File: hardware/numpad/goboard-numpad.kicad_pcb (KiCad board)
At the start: 2 copper layers, 76.3 x 110.3 mm, 45 parts, among them J1 Conn_02x05_Top_Bottom, J2 Conn_01x01, J3 Conn_01x05, SW1 SW_Push, SW10 5, SW12 2, SW13 dot, SW14 times, SW15 9, SW16 6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

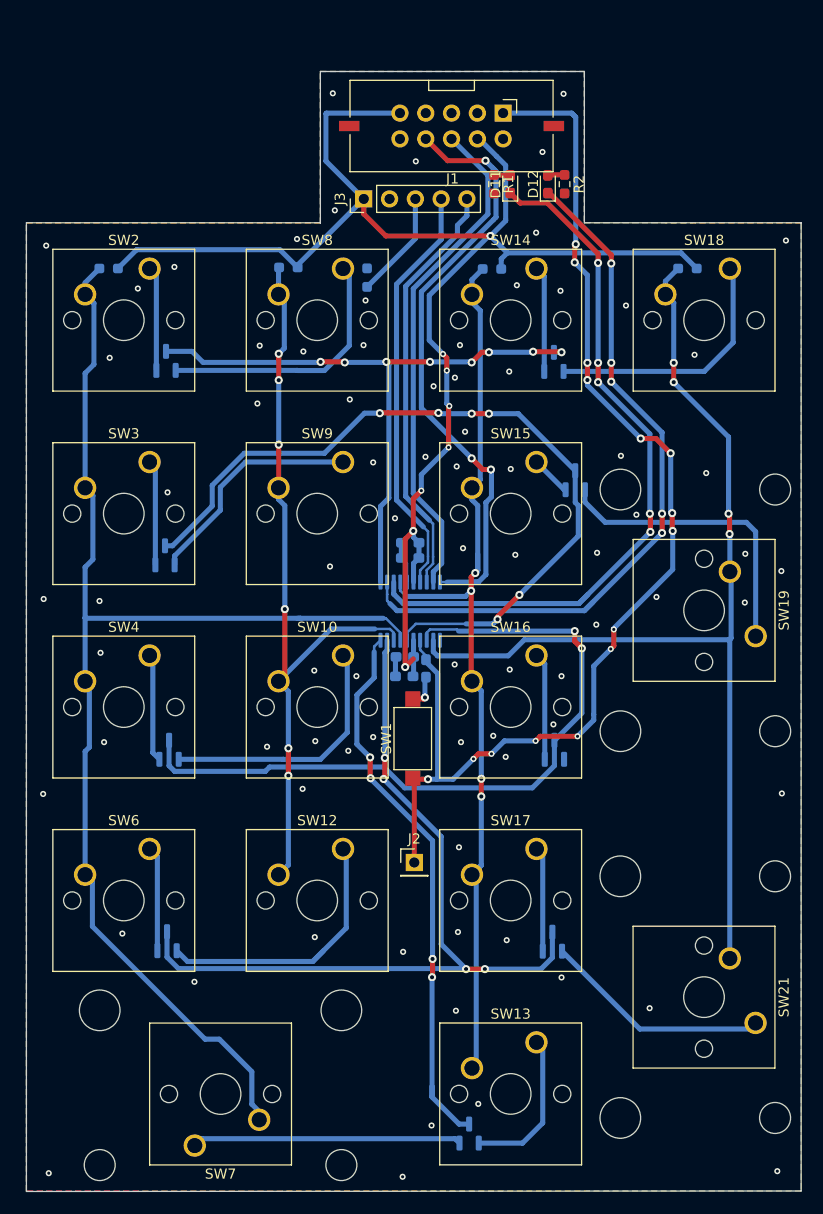
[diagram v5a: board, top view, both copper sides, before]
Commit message: Numpad: Fix DRC errors
Mainly placement of silkscreen content, track clearance violations and
overlapping courtyards.
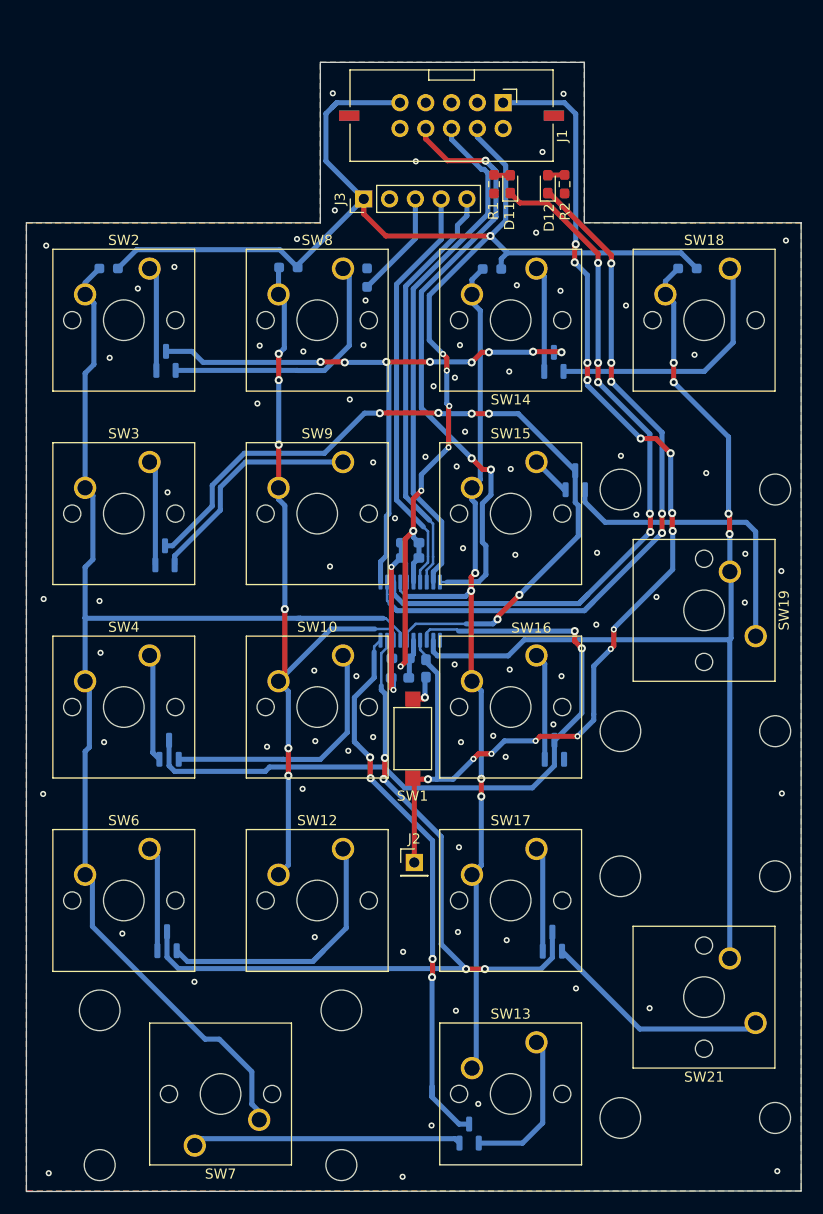
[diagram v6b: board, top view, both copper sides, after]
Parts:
- moved J1 1.02 mm to (151.5, 45.6)
- moved C5 0.45 mm to (141.3, 102.2)
- moved C2 0.45 mm to (141.4, 100.3)
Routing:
- net GND: track 9.35 -> 24.2 mm, vias 81 -> 83
- net /Keys/COLUMN_2: track 91.8 -> 90.0 mm
- net /SWDCLK: track 60.0 -> 61.3 mm
- net VCC: track 154.8 -> 156.0 mm
- net /SWDIO: track 49.7 -> 50.9 mm
- net /Keys/ROW_4: track 54.9 -> 55.4 mm
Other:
- board size 76.3 x 110.3 mm -> 76.3 x 111.2 mm

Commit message: Numpad: Fix position of the power-led
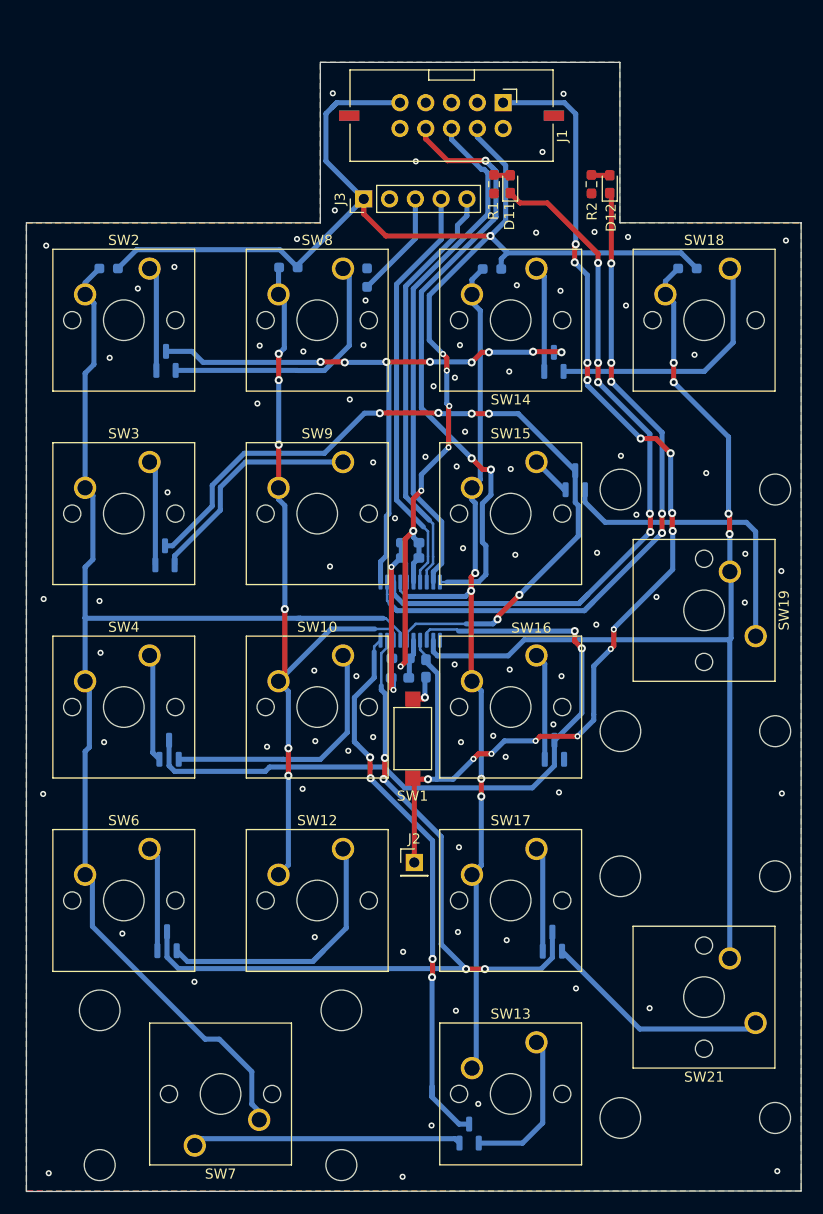
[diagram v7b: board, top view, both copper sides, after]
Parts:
- moved D12 6.10 mm to (162.0, 53.6)
- moved R2 2.65 mm to (160.2, 53.6)
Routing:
- net /mcu/LED_POWER: track 71.9 -> 69.3 mm
- net GND: vias 83 -> 86
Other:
- outline, holes or cut-outs redrawn
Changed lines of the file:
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@@
   )
   (footprint "Resistor_SMD:R_0603_1608Metric_Pad0.98x0.95mm_HandSolder" (layer "F.Cu")
-    (at 157.55 53.6 -90)
+    (at 160.2 53.6 -90)
     (descr "Resistor SMD 0603 (1608 Metric), square (rectangular) end terminal, IPC_7351 nominal with elongated pad for handsoldering. (Body size source: IPC-SM-782 page 72, https://www.pcb-3d.com/wordpress/wp-content/uploads/ipc-sm-782a_amendment_1_and_2.pdf), generated with kicad-footprint-generator")
     (tags "resistor handsolder")
@@
   )
   (footprint "Diode_SMD:D_0603_1608Metric_Pad1.05x0.95mm_HandSolder" (layer "F.Cu")
-    (at 155.9 53.6 90)
+    (at 162 53.6 90)
     (descr "Diode SMD 0603 (1608 Metric), square (rectangular) end terminal, IPC_7351 nominal, (Body size source: http://www.tortai-tech.com/upload/download/2011102023233369053.pdf), generated with kicad-footprint-generator")
     (tags "diode handsolder")
@@
   (gr_line (start 133.5 57.4) (end 104.55 57.4) (layer "Edge.Cuts") (width 0.1))
   (gr_line (start 133.5 41.6) (end 133.5 57.4) (layer "Edge.Cuts") (width 0.1))
-  (gr_line (start 159.5 57.4) (end 159.5 41.6) (layer "Edge.Cuts") (width 0.1))
-  (gr_line (start 159.5 41.6) (end 133.5 41.6) (layer "Edge.Cuts") (width 0.1))
+  (gr_line (start 163 57.4) (end 163 41.6) (layer "Edge.Cuts") (width 0.1))
+  (gr_line (start 163 41.6) (end 133.5 41.6) (layer "Edge.Cuts") (width 0.1))
   (gr_line (start 104.55 57.4) (end 104.55 152.8) (layer "Edge.Cuts") (width 0.1))
   (gr_line (start 180.85 152.75) (end 180.85 57.4) (layer "Edge.Cuts") (width 0.1))
-  (gr_line (start 180.85 57.4) (end 159.5 57.4) (layer "Edge.Cuts") (width 0.1))
+  (gr_line (start 180.85 57.4) (end 163 57.4) (layer "Edge.Cuts") (width 0.1))
   (segment (start 131.55 96.35) (end 131.25 96.35) (width 0.5) (layer "B.Cu") (net 1))
   (segment (start 110.33125 72.21875) (end 111.2 71.35) (width 0.5) (layer "B.Cu") (net 1))
@@
   (via (at 121.1 132.15) (size 0.6) (drill 0.3) (layers "F.Cu" "B.Cu") (free) (net 28))
   (via (at 147.55 89.45) (size 0.6) (drill 0.3) (layers "F.Cu" "B.Cu") (free) (net 28))
+  (via (at 157 113.5) (size 0.6) (drill 0.3) (layers "F.Cu" "B.Cu") (free) (net 28))
   (via (at 141.6 151.35) (size 0.6) (drill 0.3) (layers "F.Cu" "B.Cu") (free) (net 28))
   (via (at 147.75 77.975) (size 0.6) (drill 0.3) (layers "F.Cu" "B.Cu") (free) (net 28))
@@
   (via (at 179.35 59.15) (size 0.6) (drill 0.3) (layers "F.Cu" "B.Cu") (free) (net 28))
   (via (at 131.75 113.15) (size 0.6) (drill 0.3) (layers "F.Cu" "B.Cu") (free) (net 28))
+  (via (at 160.5 58.3) (size 0.6) (drill 0.3) (layers "F.Cu" "B.Cu") (free) (net 28))
   (via (at 171.5 82.05) (size 0.6) (drill 0.3) (layers "F.Cu" "B.Cu") (free) (net 28))
   (via (at 127.525 69.5) (size 0.6) (drill 0.3) (layers "F.Cu" "B.Cu") (free) (net 28))
@@
   (via (at 147.25 69.45) (size 0.6) (drill 0.3) (layers "F.Cu" "B.Cu") (free) (net 28))
   (via (at 146.925 81.4) (size 0.6) (drill 0.3) (layers "F.Cu" "B.Cu") (free) (net 28))
+  (via (at 163.8 58.8) (size 0.6) (drill 0.3) (layers "F.Cu" "B.Cu") (free) (net 28))
   (via (at 131.825 70.075) (size 0.6) (drill 0.3) (layers "F.Cu" "B.Cu") (free) (net 28))
   (via (at 156.45 106.8) (size 0.6) (drill 0.3) (layers "F.Cu" "B.Cu") (free) (net 28))
@@
   (segment (start 141.4775 90.41) (end 141.4775 88.92) (width 0.5) (layer "B.Cu") (net 28))
   (segment (start 162.15 73.05) (end 162.15 71.1875) (width 0.5) (layer "F.Cu") (net 30))
-  (segment (start 156.052698 54.475) (end 155.9 54.475) (width 0.5) (layer "F.Cu") (net 30))
-  (segment (start 162.15 60.572302) (end 156.052698 54.475) (width 0.5) (layer "F.Cu") (net 30))
-  (segment (start 162.15 61.4) (end 162.15 60.572302) (width 0.5) (layer "F.Cu") (net 30))
+  (segment (start 162.15 61.4) (end 162.15 54.625) (width 0.5) (layer "F.Cu") (net 30))
+  (segment (start 162.15 54.625) (end 162 54.475) (width 0.5) (layer "F.Cu") (net 30))
   (segment (start 167.15 87.95) (end 167.15 86.05) (width 0.5) (layer "F.Cu") (net 30))
   (via (at 162.15 71.1875) (size 0.8) (drill 0.4) (layers "F.Cu" "B.Cu") (net 30))
@@
   (segment (start 150.6375 52.725) (end 150.6 52.6875) (width 0.5) (layer "F.Cu") (net 37))
   (segment (start 152.2 52.725) (end 150.6375 52.725) (width 0.5) (layer "F.Cu") (net 37))
-  (segment (start 155.9375 52.6875) (end 155.9 52.725) (width 0.5) (layer "F.Cu") (net 38))
-  (segment (start 157.55 52.6875) (end 155.9375 52.6875) (width 0.5) (layer "F.Cu") (net 38))
+  (segment (start 160.2375 52.725) (end 160.2 52.6875) (width 0.5) (layer "F.Cu") (net 38))
+  (segment (start 162 52.725) (end 160.2375 52.725) (width 0.5) (layer "F.Cu") (net 38))
   (segment (start 158.55 97.612489) (end 158.55 98.612489) (width 0.5) (layer "F.Cu") (net 39))
   (segment (start 158.55 98.612489) (end 159.25 99.312489) (width 0.5) (layer "F.Cu") (net 39))
@@
     (polygon
       (pts
-        (xy 159.5 57.4)
+        (xy 163 57.4)
         (xy 180.85 57.45)
         (xy 180.85 152.75)
@@
         (xy 133.5 57.45)
         (xy 133.5 41.6)
-        (xy 159.5 41.6)
+        (xy 163 41.6)
       )
     )

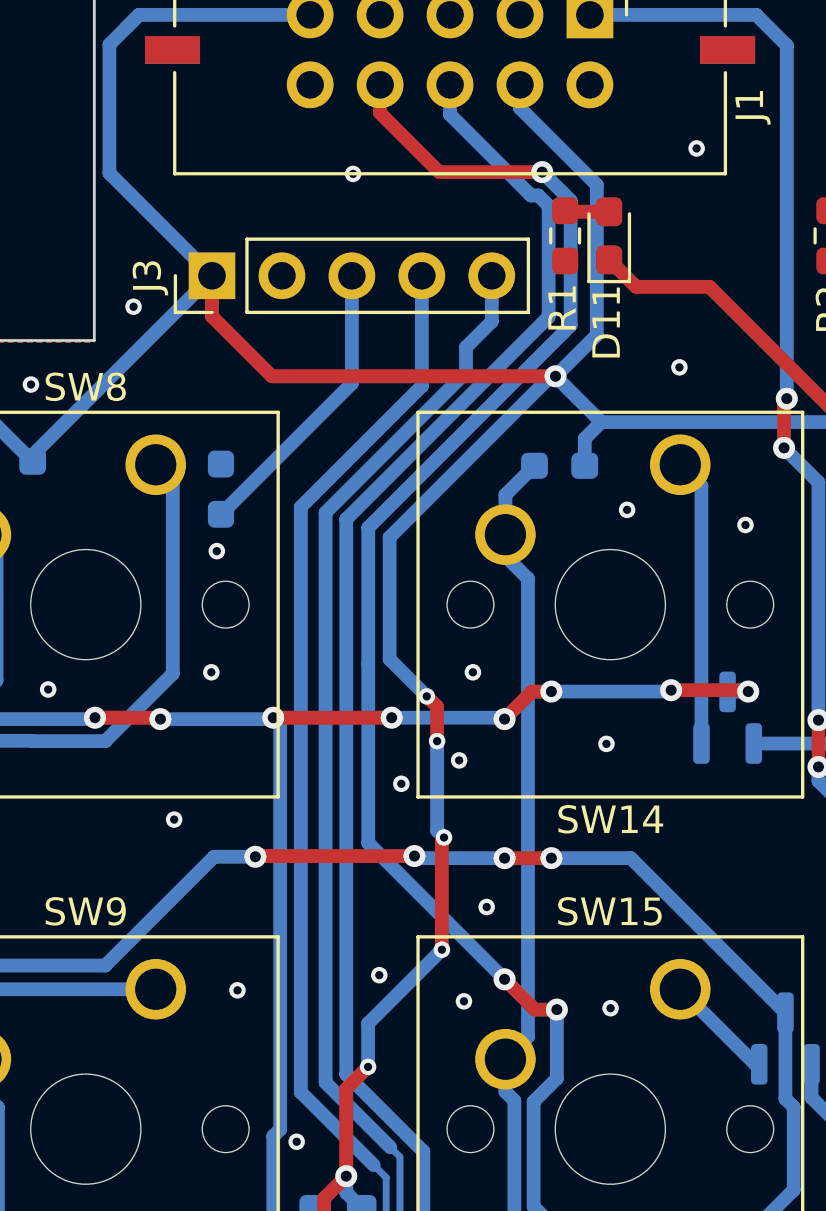
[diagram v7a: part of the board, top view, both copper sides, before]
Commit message: Improve routing of a track
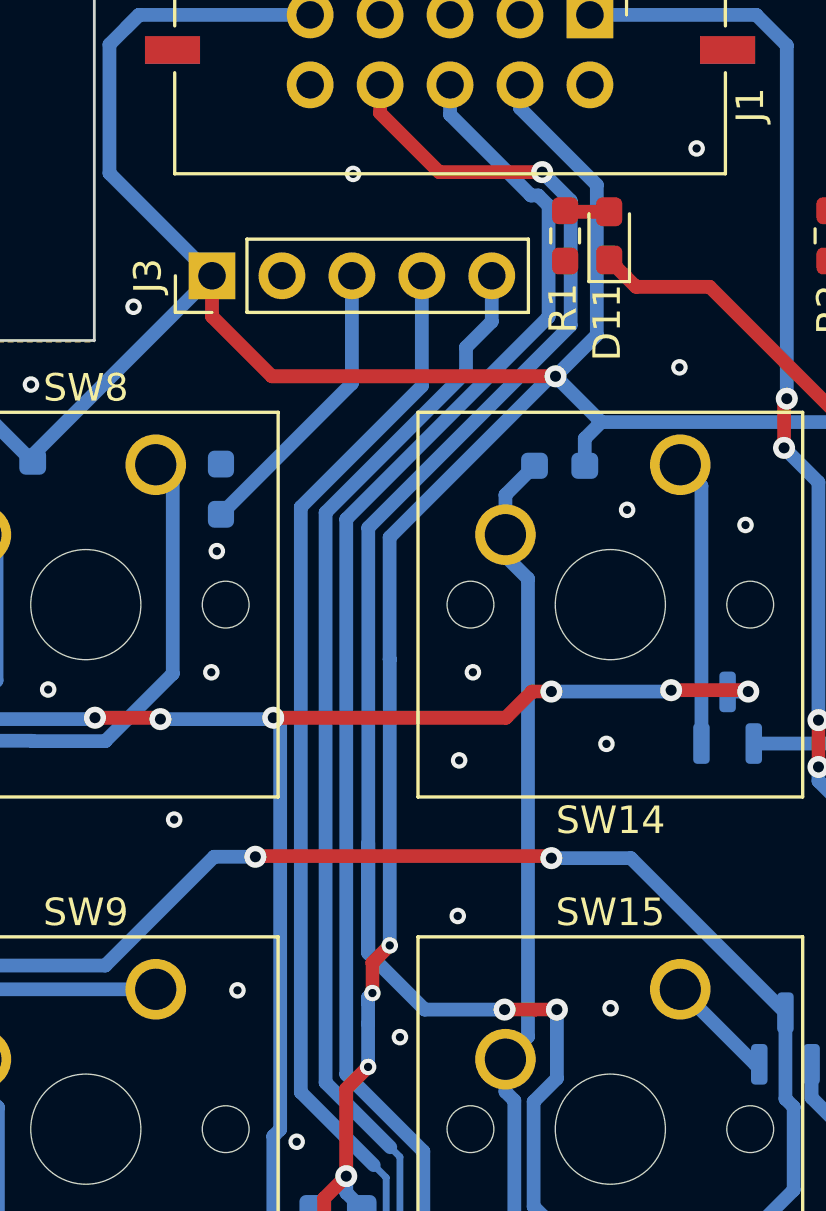
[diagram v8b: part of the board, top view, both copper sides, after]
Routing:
- net /SWDCLK: track 61.3 -> 67.7 mm
- net VCC: track 156.0 -> 154.4 mm, vias 8 -> 6
- net /Keys/ROW_0: vias 8 -> 6
- net GND: vias 86 -> 84
- net /Keys/ROW_1: vias 6 -> 4
